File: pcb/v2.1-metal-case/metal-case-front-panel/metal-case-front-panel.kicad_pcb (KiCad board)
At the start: 2 copper layers, 50 x 20 mm, 5 parts

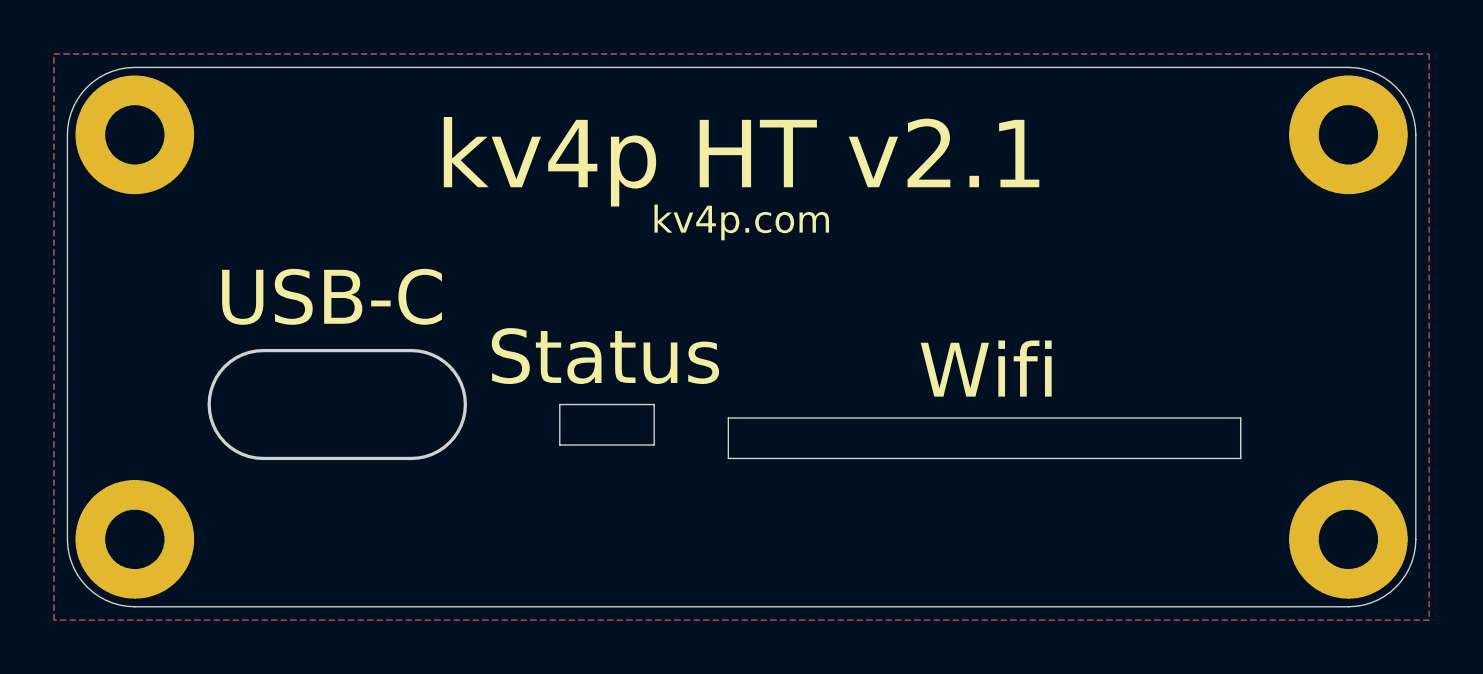
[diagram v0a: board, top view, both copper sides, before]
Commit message: v2.1b as ordered 2025-04-17. VHF and UHF #22. SAO headers. PTT buttons. User LED.
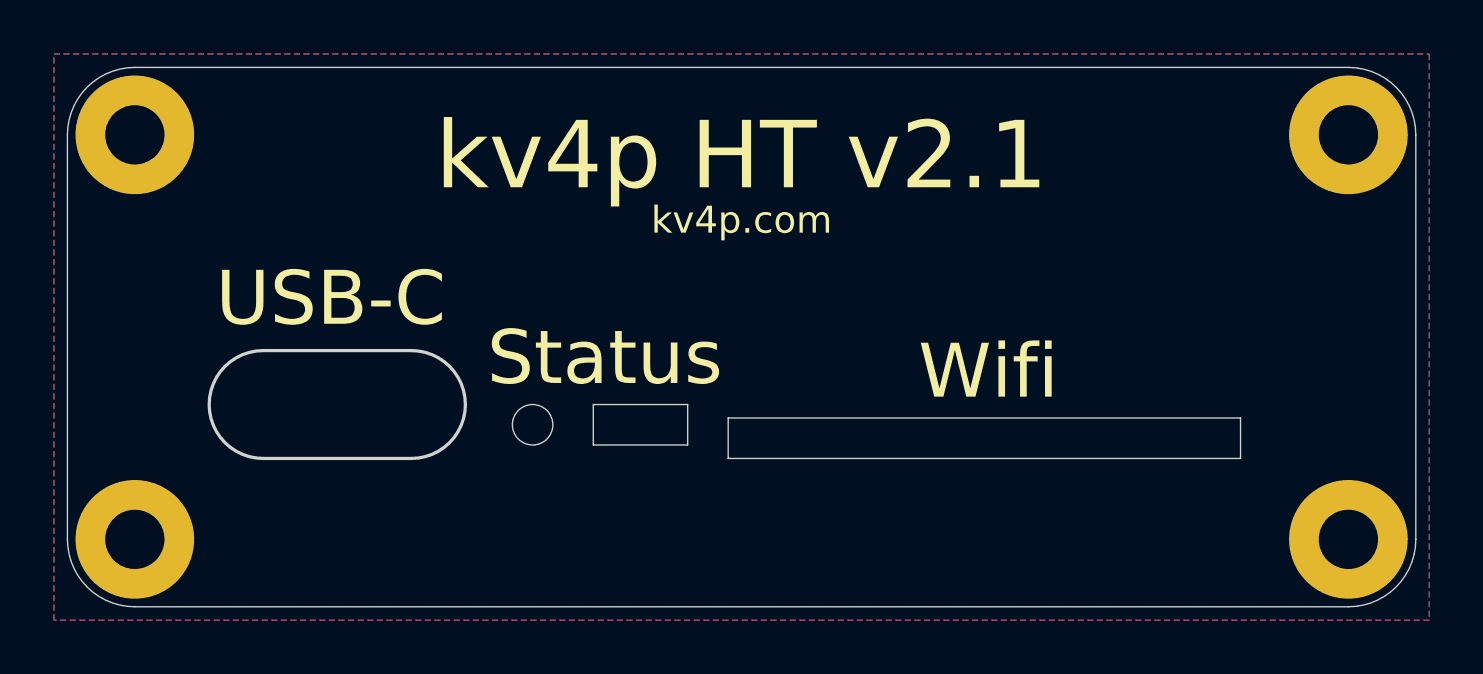
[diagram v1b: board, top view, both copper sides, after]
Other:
- outline, holes or cut-outs redrawn
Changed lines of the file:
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@@
 	)
 	(gr_rect
-		(start 120.75674 108.25)
-		(end 124.25674 109.75)
+		(start 122 108.25)
+		(end 125.5 109.75)
+		(stroke
+			(width 0.05)
+			(type default)
+		)
+		(fill none)
+		(layer "Edge.Cuts")
+	)
+	(gr_circle
+		(center 119.75 109)
+		(end 120.5 109)
 		(stroke
 			(width 0.05)
@@
 	)
 	(gr_rect
-		(start 127.00722 108.75)
-		(end 146.00722 110.25)
+		(start 127 108.75)
+		(end 146 110.25)
 		(stroke
 			(width 0.05)
